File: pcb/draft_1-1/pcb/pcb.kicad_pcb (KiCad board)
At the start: 2 copper layers, 1 part, among them U1 ATSAML21G18B-AUT

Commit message: paper cut out trade study
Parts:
- added BT1: Battery, lir2032:LIR2032, B.Cu at (140.5, 69.7)
- added FID1: Fiducial, Fiducial:Fiducial_0.5mm_Mask1mm, F.Cu at (131.0, 45.2)
- added FID2: Fiducial, Fiducial:Fiducial_0.5mm_Mask1mm, F.Cu at (177.9, 44.5)
- added FID3: Fiducial, Fiducial:Fiducial_0.5mm_Mask1mm, F.Cu at (178.7, 87.3)
- added IC1: BQ21061YFPR, BQ25155:BGA20C40P4X5_162X202X50, F.Cu at (143.0, 46.3)
- added J1: XF2M-2415-1A, XF2M-2415-1A:OMRON_XF2M-2415-1A, F.Cu at (171.8, 59.6)
- added J2: 10118194-0001LF, 10118194-0001LF:AMPHENOL_10118194-0001LF, F.Cu at (154.2, 42.8)
- added LS2: SP-1511S-6, SP-1511S-6:SP-1511S-6_ALT, F.Cu at (169.6, 79.3)
- added S1: TL3315NF100Q, TL3315NF100Q:TL3315NF100Q, F.Cu at (131.4, 50.4)
- added U2: TPD4S012DRYR, TPD4S012DRYR:SON50P100X145X60-6N, F.Cu at (151.8, 47.8)
- added U3: IIS2DLPC, Package_LGA:LGA-12_2x2mm_P0.5mm, F.Cu at (139.1, 51.4)
- added U4: AT25SF641, Package_SO:SOIC-8_5.275x5.275mm_P1.27mm, F.Cu at (168.6, 46.0)
- added U5: XZMDKCBDDG45S-9, XZMDKCBDDG45S-9:PLCC-4, F.Cu at (154.6, 79.3)
- added U6: eInk_waveshare_1.54A, custom:eInk_waveshare_1.54A, B.Cu at (154.0, 60.8)
- U1: value ATSAML21G18B-AUT -> ATSAML21J18B-AUT; footprint Package_QFP:TQFP-48_7x7mm_P0.5mm -> Package_QFP:TQFP-64_10x10mm_P0.5mm
- moved U1 43.1 mm to (154.9, 57.4)
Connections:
- U1 pad 33: Net-(U1-Pad33) -> Net-(U1-Pad22)
- U1 pad 34: Net-(U1-Pad34) -> Net-(U1-Pad21)
- U1 pad 35: Net-(U1-Pad18) -> Net-(U1-Pad35)
- U1 pad 36: Net-(U1-Pad17) -> Net-(U1-Pad36)
- U1 pad 42: Net-(U1-Pad18) -> Net-(U1-Pad42)
- U1 pad 45: Net-(U1-Pad45) -> D-
- U1 pad 46: Net-(U1-Pad46) -> D+
- U1 pad 47: Net-(U1-Pad47) -> Net-(U1-Pad22)
- U1 pad 48: Net-(U1-Pad48) -> Net-(U1-Pad21)
- U1 pad 7: Net-(U1-Pad7) -> Net-(U1-Pad22)
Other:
- board outline added: 54 x 85.6 mm
- net class Default: clearance 0.2 -> 0.15; trace_width 0.25 -> 0.1524; via_dia 0.8 -> 0.508; via_drill 0.4 -> 0.254
- rule trace_clearance: 0.2 -> 0.15
- rule trace_min: 0.2 -> 0.1524
- rule via_min_drill: 0.3 -> 0.254
- rule via_min_size: 0.4 -> 0.508

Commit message: paper cutout study
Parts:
- removed LS2: SP-1511S-6, SP-1511S-6:SP-1511S-6_ALT
- added D1: D, Diode_SMD:D_SOD-123, F.Cu at (168.4, 46.9)
- added D2: D, Diode_SMD:D_SOD-123, F.Cu at (164.9, 64.9)
- added D3: D, Diode_SMD:D_SOD-123, F.Cu at (165.2, 67.8)
- added D4: D, Diode_SMD:D_SOD-123, F.Cu at (165.1, 61.6)
- added L1: L, Inductor_SMD:L_1206_3216Metric, F.Cu at (164.9, 57.8)
- added LS1: CMT-8503-90-SMT-TR, CMT-8503-90-SMT-TR:XDCR_CMT-8503-90-SMT-TR, F.Cu at (175.2, 47.1)
- added Q1: SI1308EDL-T1-GE3, Package_TO_SOT_SMD:SOT-323_SC-70, F.Cu at (164.6, 53.2)
- moved U4 36.1 mm to (133.5, 54.4), turned to 180 degrees
- moved FID2 9.90 mm to (168.1, 43.1)
- moved S1 5.84 mm to (134.9, 45.7)
- moved U3 3.59 mm to (142.6, 52.2)
- moved FID1 2.83 mm to (129.0, 43.2)
- moved IC1 1.90 mm to (144.9, 46.4)
- moved J1 1.48 mm to (172.8, 60.7)
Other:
- board text added: "v1.1"

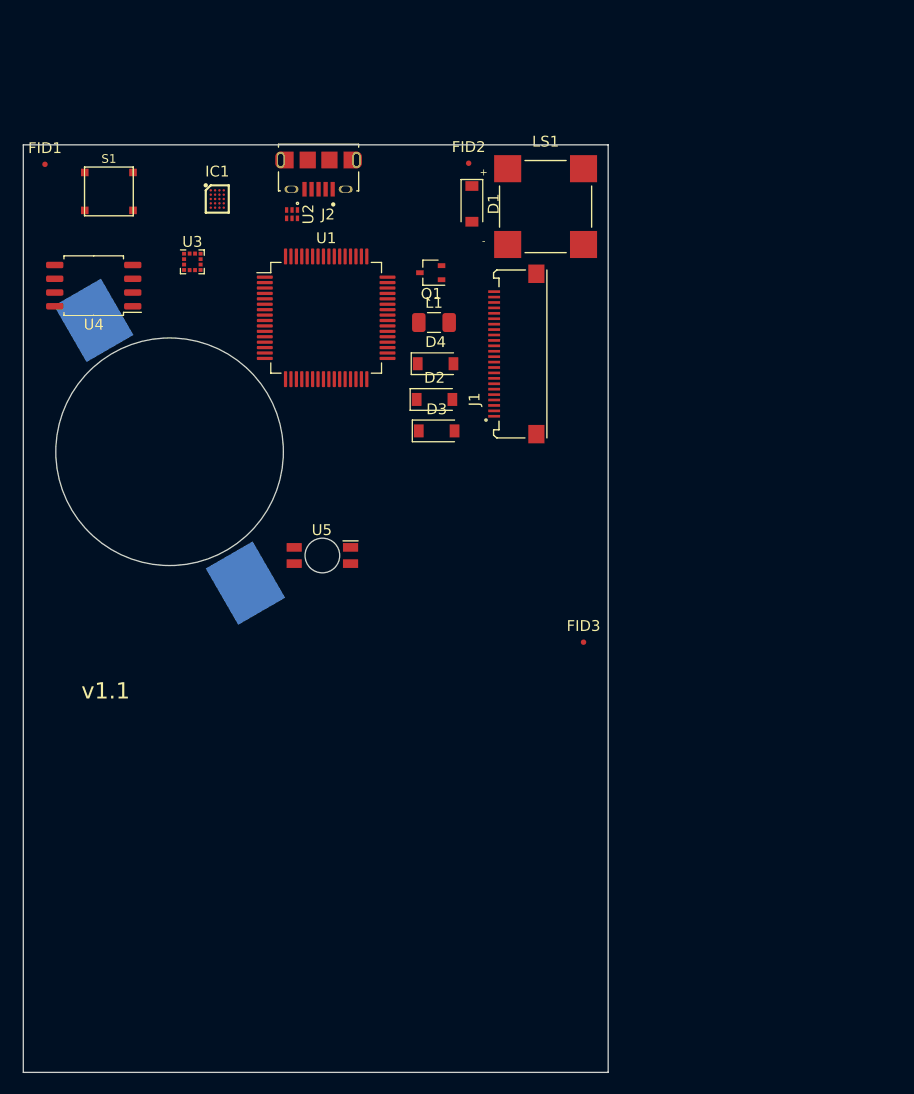
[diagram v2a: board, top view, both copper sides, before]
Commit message: trade study on speaker
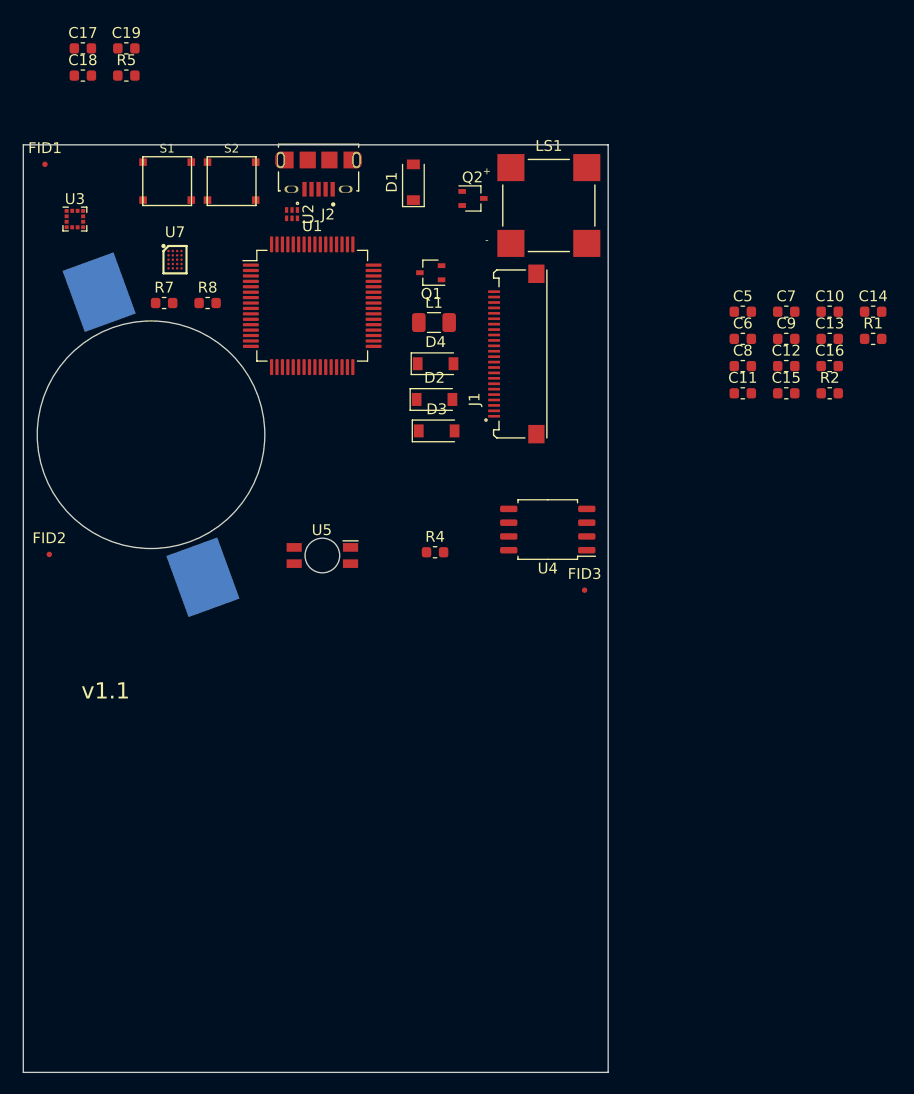
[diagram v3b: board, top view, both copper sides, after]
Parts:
- removed IC1: BQ21061YFPR, BQ25155:BGA20C40P4X5_162X202X50
- added C10: 1uF, Capacitor_SMD:C_0603_1608Metric, F.Cu at (201.4, 56.8)
- added C11: 1uF, Capacitor_SMD:C_0603_1608Metric, F.Cu at (193.4, 64.3)
- added C12: 1uF, Capacitor_SMD:C_0603_1608Metric, F.Cu at (197.4, 61.8)
- added C13: 1uF, Capacitor_SMD:C_0603_1608Metric, F.Cu at (201.4, 59.3)
- added C14: 1uF, Capacitor_SMD:C_0603_1608Metric, F.Cu at (205.4, 56.8)
- added C15: 4.7uF, Capacitor_SMD:C_0603_1608Metric, F.Cu at (197.4, 64.3)
- added C16: 4.7uF, Capacitor_SMD:C_0603_1608Metric, F.Cu at (201.4, 61.8)
- added C17: 22uF, Capacitor_SMD:C_0603_1608Metric, F.Cu at (132.5, 32.5)
- added C18: 10uF, Capacitor_SMD:C_0603_1608Metric, F.Cu at (132.5, 35.0)
- added C19: 10uF, Capacitor_SMD:C_0603_1608Metric, F.Cu at (136.5, 32.5)
- added C5: 1uF, Capacitor_SMD:C_0603_1608Metric, F.Cu at (193.4, 56.8)
- added C6: 1uF, Capacitor_SMD:C_0603_1608Metric, F.Cu at (193.4, 59.3)
- added C7: 100nF, Capacitor_SMD:C_0603_1608Metric, F.Cu at (197.4, 56.8)
- added C8: 1uF, Capacitor_SMD:C_0603_1608Metric, F.Cu at (193.4, 61.8)
- added C9: 1uF, Capacitor_SMD:C_0603_1608Metric, F.Cu at (197.4, 59.3)
- added Q2: SI1308EDL-T1-GE3, Package_TO_SOT_SMD:SOT-323_SC-70, F.Cu at (168.5, 46.4)
- added R1: 10k, Resistor_SMD:R_0603_1608Metric, F.Cu at (205.4, 59.3)
- added R2: 3R0, Resistor_SMD:R_0603_1608Metric, F.Cu at (201.4, 64.3)
- added R4: 68R0, Resistor_SMD:R_0603_1608Metric, F.Cu at (165.0, 79.0)
- added R5: 10k, Resistor_SMD:R_0603_1608Metric, F.Cu at (136.5, 35.0)
- added R7: 10k, Resistor_SMD:R_0603_1608Metric, F.Cu at (140.0, 56.0)
- added R8: 10k, Resistor_SMD:R_0603_1608Metric, F.Cu at (144.0, 56.0)
- added S2: TL3315NF100Q, TL3315NF100Q:TL3315NF100Q, F.Cu at (146.2, 44.8)
- added U7: BQ25155, BQ21061YFPR:BGA20C40P4X5_162X202X50, F.Cu at (141.0, 52.0)
- BT1: value Battery -> 45mAh
- D1, D2, D3, D4: value D -> MBR0530
- L1: value L -> 68uH
- moved FID2 52.9 mm to (129.4, 79.2)
- moved U4 47.6 mm to (175.4, 76.9)
- moved U3 11.5 mm to (131.8, 48.2)
- moved D1 5.76 mm to (163.0, 44.9), turned to 90 degrees
- moved S1 5.46 mm to (140.3, 44.8)
- moved FID3 4.80 mm to (178.8, 82.5)
- moved BT1 2.32 mm to (138.8, 68.2), turned to 110 degrees
- moved U1 1.70 mm to (153.7, 56.2)
- moved LS1 0.32 mm to (175.5, 47.0)
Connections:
- net Net-(J1-Pad10) renamed eRST
- net Net-(J1-Pad11) renamed eDC
- net Net-(J1-Pad12) renamed eCS
- net Net-(J1-Pad13) renamed eCLK
- net Net-(J1-Pad9) renamed eBUSY
- net Net-(U3-Pad11) renamed INT_ACC_2
- net Net-(U3-Pad12) renamed INT_ACC_1
- net Net-(U4-Pad1) renamed fCS
- net Net-(U4-Pad5) renamed fSDI
- net Net-(U5-Pad3) renamed BLUE
- net Net-(U5-Pad4) renamed GREEN
- net ~RESET renamed Net-(C3-Pad1)
- D1 pad 1: Net-(D1-Pad1) -> +3V3
- D2 pad 1: Net-(D2-Pad1) -> ePREVGH
- D2 pad 2: Net-(D2-Pad2) -> Net-(C16-Pad1)
- D3 pad 1: Net-(D3-Pad1) -> Net-(C16-Pad2)
- D3 pad 2: Net-(D3-Pad2) -> ePREVGL
- D4 pad 1: Net-(D4-Pad1) -> eBS
- D4 pad 2: Net-(D4-Pad2) -> Net-(C16-Pad2)
- J1 pad 14: Net-(J1-Pad14) -> eDIN
- J1 pad 15: Net-(J1-Pad15) -> +3V3
- J1 pad 16: Net-(J1-Pad16) -> +3V3
- J1 pad 17: Net-(J1-Pad17) -> eBS
- J1 pad 2: Net-(J1-Pad2) -> eGDR
- J1 pad 21: Net-(J1-Pad21) -> ePREVGH
- J1 pad 23: Net-(J1-Pad23) -> ePREVGL
- J1 pad 3: Net-(J1-Pad3) -> eRESE
- J1 pad 8: Net-(J1-Pad8) -> eBS
- J2 pad 5: GND -> eBS
- L1 pad 1: Net-(L1-Pad1) -> Net-(C16-Pad1)
- L1 pad 2: Net-(L1-Pad2) -> +3V3
- LS1 pad N: Net-(LS1-PadN) -> Net-(D1-Pad2)
- LS1 pad P: Net-(LS1-PadP) -> +3V3
- Q1 pad 1: Net-(Q1-Pad1) -> eGDR
- Q1 pad 2: Net-(Q1-Pad2) -> eRESE
- Q1 pad 3: Net-(Q1-Pad3) -> Net-(C16-Pad1)
- S1 pad 3: Net-(S1-Pad3) -> eBS
- S1 pad 4: Net-(S1-Pad3) -> eBS
- U1 pad 22: Net-(U1-Pad22) -> eBS
- U1 pad 33: Net-(U1-Pad22) -> eBS
- U1 pad 47: Net-(U1-Pad22) -> eBS
- U1 pad 54: Net-(U1-Pad22) -> eBS
- U1 pad 59: Net-(U1-Pad59) -> SDA_1V8
- U1 pad 60: Net-(U1-Pad60) -> SCL_1V8
- U1 pad 7: Net-(U1-Pad22) -> eBS
- U2 pad 4: GND -> eBS
- U3 pad 1: SCL -> SCL_1V8
- U3 pad 10: Net-(U3-Pad10) -> +1V8
- U3 pad 4: SDA -> SDA_1V8
- U3 pad 5: Net-(U3-Pad5) -> eBS
- U3 pad 6: Net-(U3-Pad6) -> eBS
- U3 pad 7: GND -> eBS
- U3 pad 8: GND -> eBS
- U3 pad 9: Net-(U3-Pad9) -> +1V8
- U4 pad 2: Net-(U4-Pad2) -> eDIN
- U4 pad 4: Net-(U4-Pad4) -> eBS
- U4 pad 8: Net-(U4-Pad8) -> +3V3
- U5 pad 2: Net-(U5-Pad2) -> +3V3
